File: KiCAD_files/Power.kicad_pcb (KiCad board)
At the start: 2 copper layers, 92 x 100 mm, 93 parts, among them J1 2604-1102, J2 2604-1102, J3 Power_Board_outline, J4 2604-1102, J5 2604-1102, Q1 QM6006D, Q2 QM6006D, Q3 Q_NIGBT_GCE, Q4 QM6006D, Q5 QM6006D, U1 ACS730xLCTR-20AB, U2 LM35-LP, U3 ACS712xLCTR-20A, U4 ACS730xLCTR-20AB

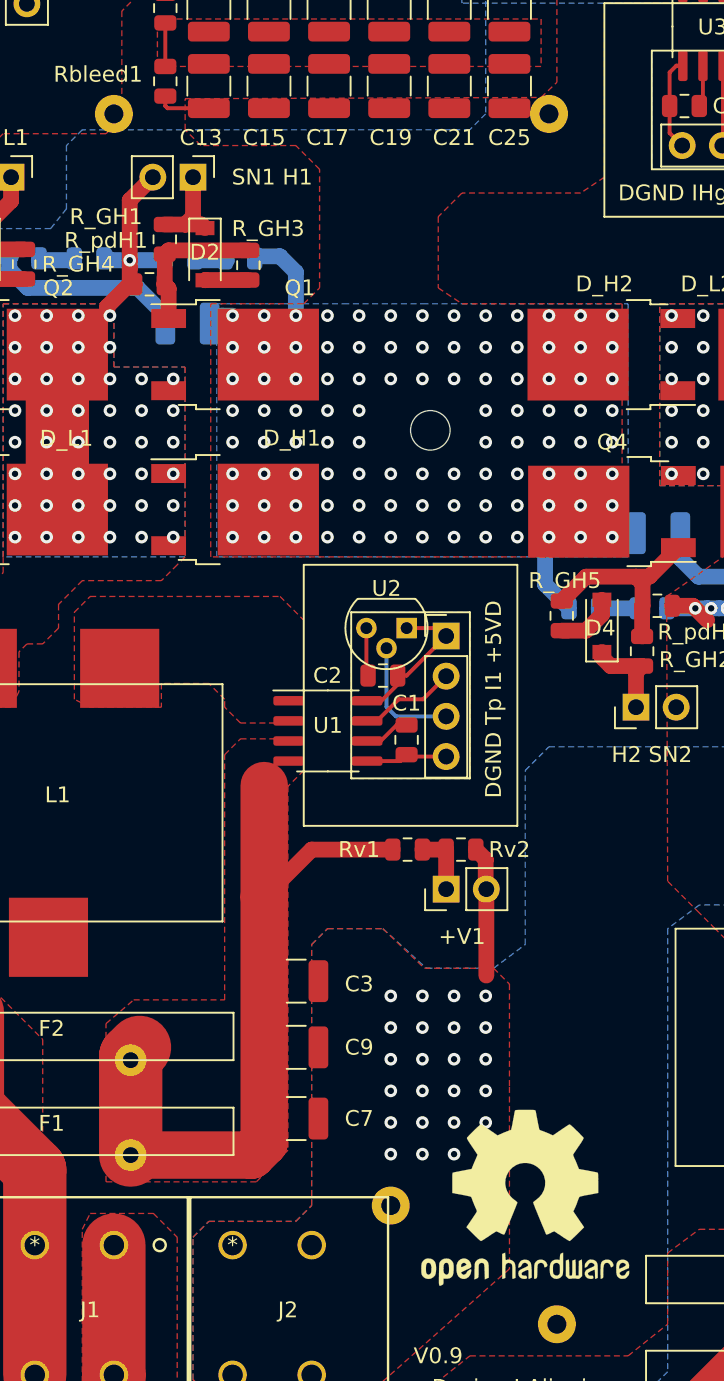
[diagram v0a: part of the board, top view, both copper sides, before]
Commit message: Updated values in pcbnew - regenerated interactive BOM
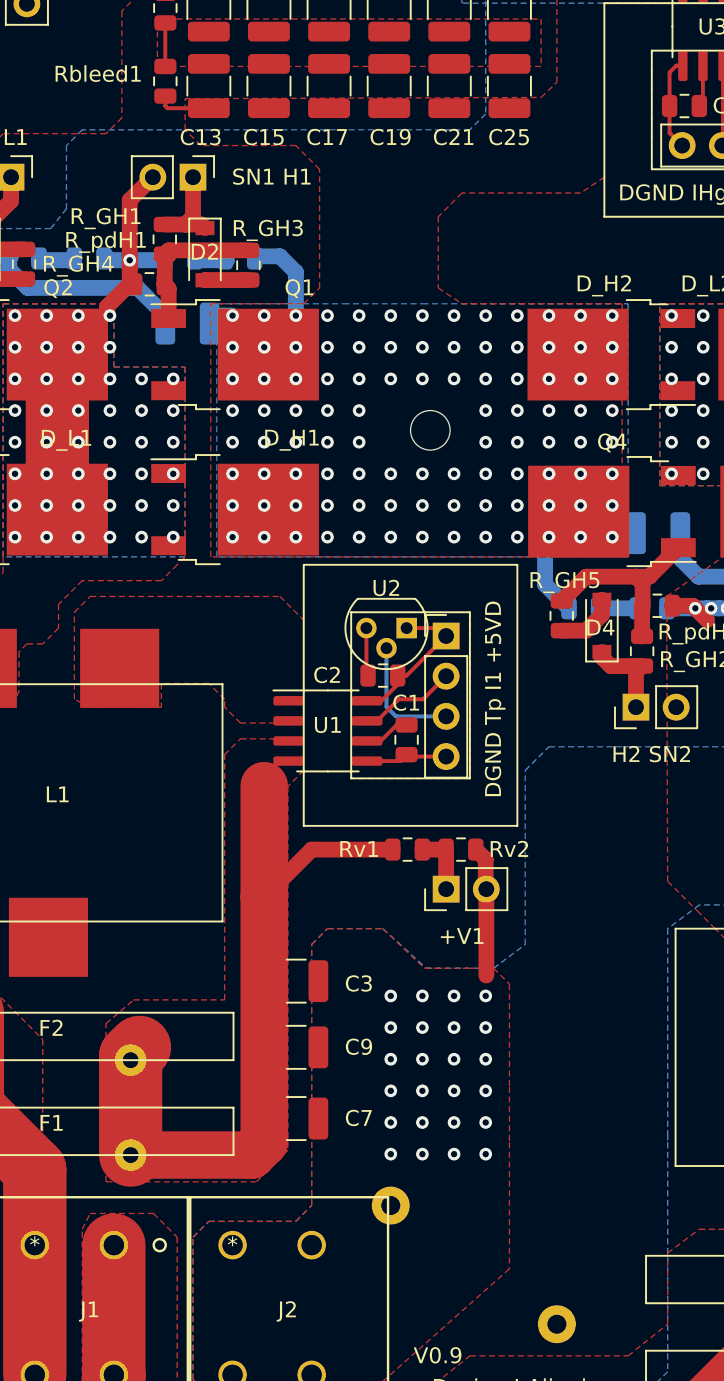
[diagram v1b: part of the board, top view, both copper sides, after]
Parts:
- removed CFilmOut: C_Rect_L31.5mm_W20.0mm_P27.50mm_MKS4, Capacitor_THT:C_Rect_L31.5mm_W20.0mm_P27.50mm_MKS4
- removed the REF** at (86.0, 122.5)
- D2, D3, D4, D5: value D -> STPS0520Z
- D_H1, D_H2, D_L1, D_L2: value D_Schottky_AKA -> STTH1002C
- F1, F2, F3, F4: value Polyfuse -> Polyfuse RKEF500
- Q1, Q2, Q4, Q5: value QM6006D -> IRFR4615
- Q3: value Q_NIGBT_GCE -> FGD3040G2-F085
- Rv1, Rv3: value R_Small -> 150K
- Rv2, Rv4: value R_Small -> 470
- Rv5: value R_Small -> 330K
- Rv6: value R_Small -> 5.6K

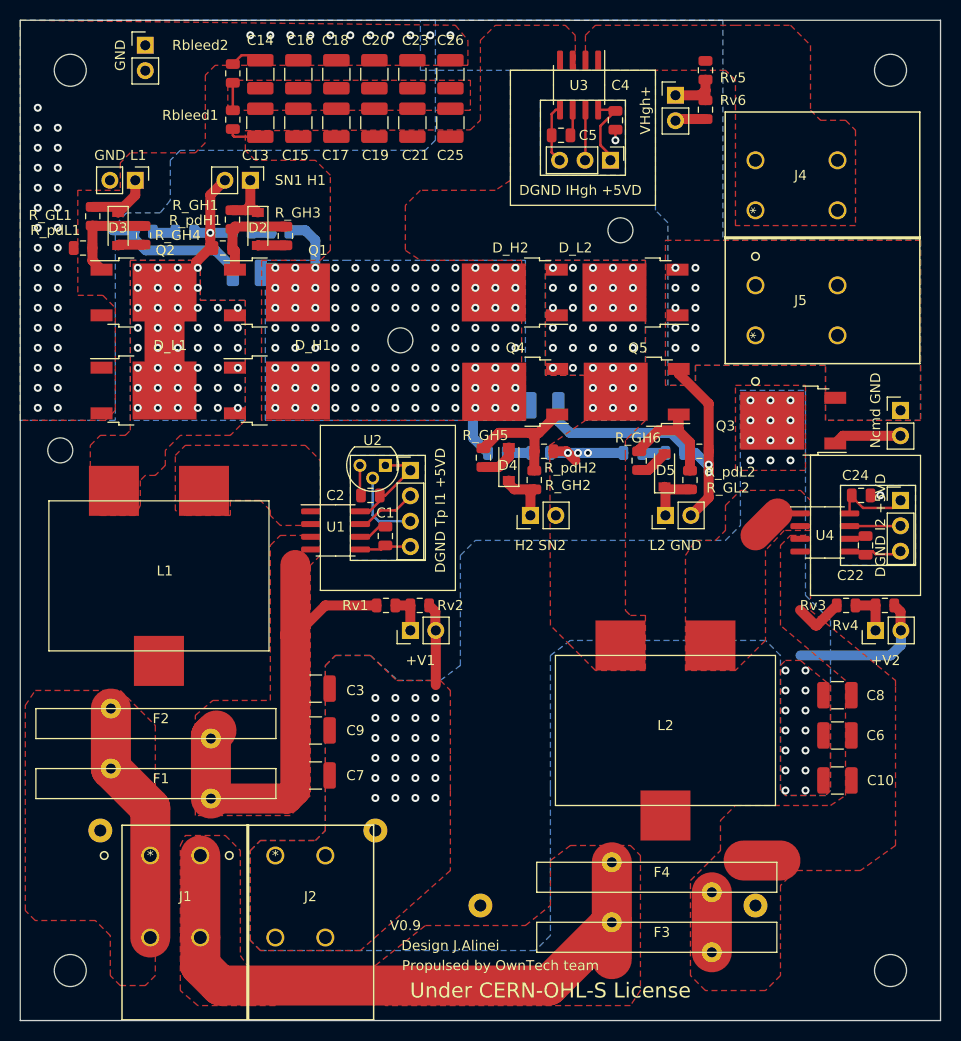
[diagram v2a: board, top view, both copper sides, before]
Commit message: Added RKEF500 3D footprints
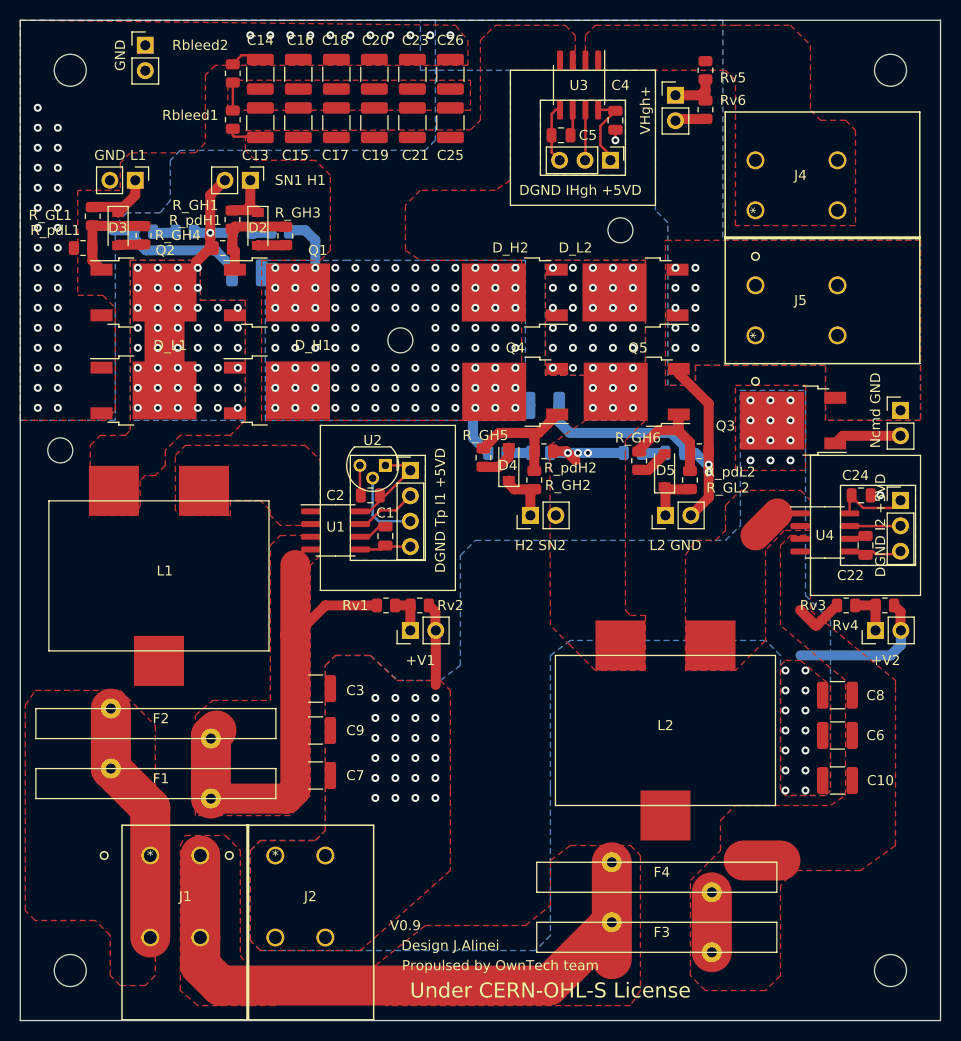
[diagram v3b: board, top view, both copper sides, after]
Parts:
- removed CFilm1, CFilm2: C_Rect_L31.5mm_W20.0mm_P27.50mm_MKS4, Capacitor_THT:C_Rect_L31.5mm_W20.0mm_P27.50mm_MKS4
